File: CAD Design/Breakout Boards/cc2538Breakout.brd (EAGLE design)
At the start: 160 x 100 mm, 21 parts

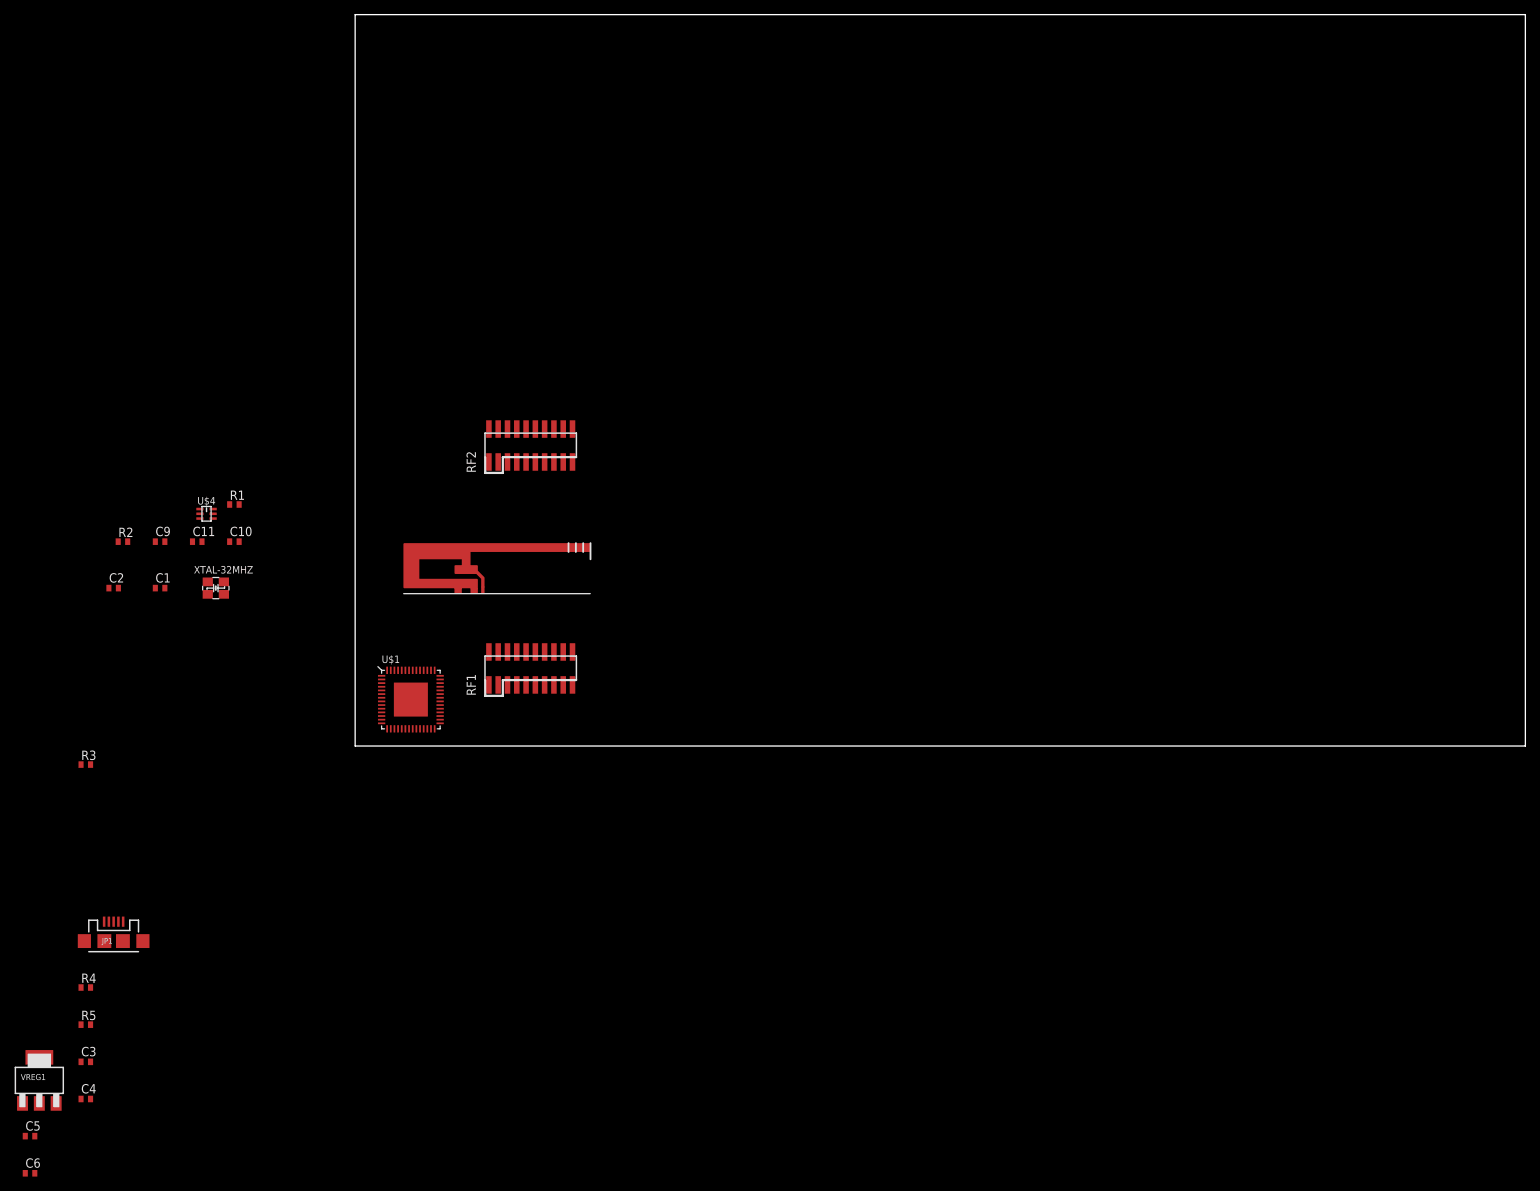
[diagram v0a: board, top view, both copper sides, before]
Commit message: cc2538EM schematic finished
Pin matched headers, added VCC decoupling bank.  Ready for board layout.
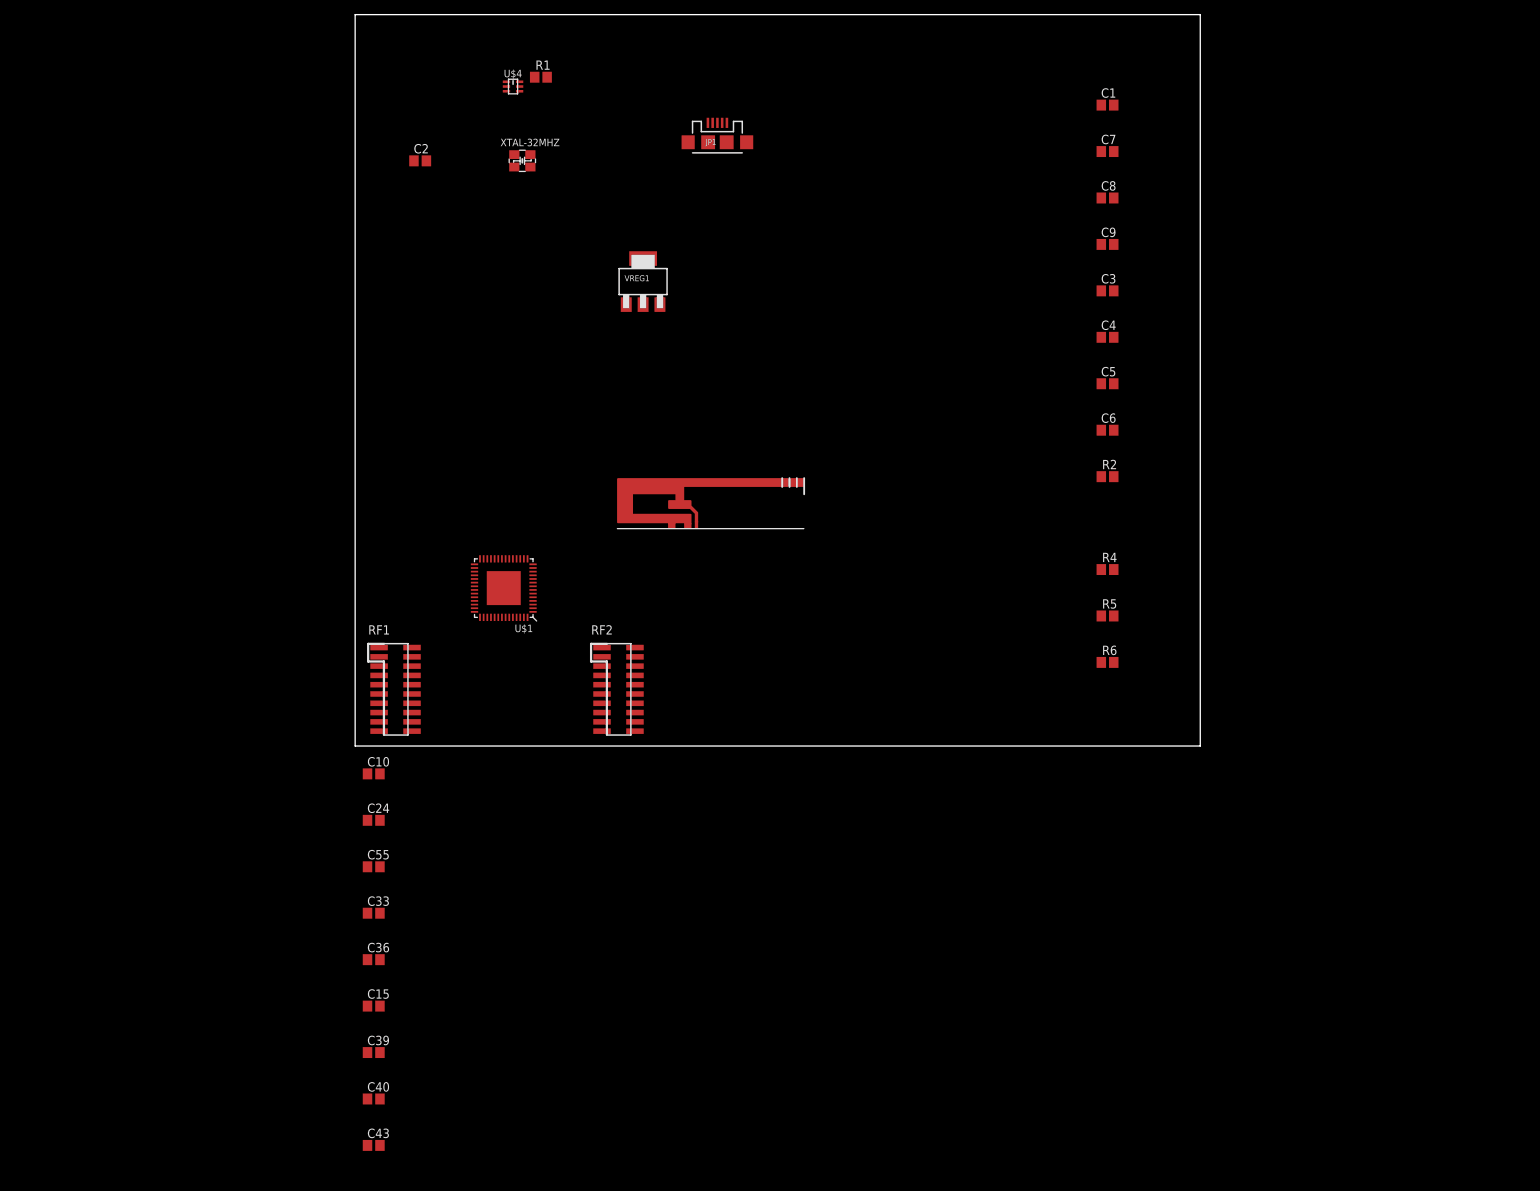
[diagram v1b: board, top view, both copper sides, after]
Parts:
- removed C11: 1nF, PCB 3.0.0:DISCRETE_C0402
- removed R3: 56k, PCB 3.0.0:RCL_R0402
- added C15, C24, C33, C36, C43: 100nF, resistor:C0805
- added C39, C55, C7, C8: 1uF, resistor:C0805
- added C40: 100pF, resistor:C0805
- added R6: 56k, resistor:R0805
- C1, C2, C3, C4: device PCB 3.0.0:DISCRETE_C0402 -> resistor:C0805
- C10: value 1uF -> 100nF; device PCB 3.0.0:DISCRETE_C0402 -> resistor:C0805
- C5, C6: value .1uF -> 1uF; device PCB 3.0.0:DISCRETE_C0402 -> resistor:C0805
- C9: value 1uF -> 1nF; device PCB 3.0.0:DISCRETE_C0402 -> resistor:C0805
- R1, R2, R4, R5: device PCB 3.0.0:RCL_R0402 -> resistor:R0805
- moved C5 179.7 mm to (102.9, 49.5)
- moved C6 179.0 mm to (102.9, 43.2)
- moved C3 175.0 mm to (102.9, 62.2)
- moved C4 174.2 mm to (102.9, 55.9)
- moved R4 150.9 mm to (102.9, 24.1)
- moved R5 150.5 mm to (102.9, 17.8)
- moved C1 145.4 mm to (102.9, 87.6)
- moved JP1 136.9 mm to (49.5, 82.5)
- moved VREG1 136.9 mm to (39.4, 63.5)
- moved C9 135.8 mm to (102.9, 68.6)
- moved R2 134.9 mm to (102.9, 36.8)
- moved C2 71.9 mm to (8.89, 80.0)
- moved U$4 71.9 mm to (21.6, 90.2)
- moved XTAL-32MHZ 71.9 mm to (22.9, 80.0)
- moved R1 71.9 mm to (25.4, 91.4)
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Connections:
- removed net N$12: U$1.23
- removed net N$15: U$1.22
- removed net N$16: U$1.21
- removed net N$17: U$1.20
- removed net N$18: U$1.19
- removed net N$19: U$1.18
- removed net N$21: U$1.16
- removed net N$22: U$1.5
- removed net N$23: U$1.6
- removed net N$24: U$1.7
- removed net N$25: U$1.8
- removed net N$26: U$1.9
- removed net N$27: U$1.11
- removed net N$28: U$1.12
- removed net N$29: U$1.13
- removed net N$3: U$1.31
- removed net N$31: U$1.54
- removed net N$32: U$1.53
- removed net N$33: U$1.52
- removed net N$34: U$1.51
- removed net N$35: U$1.50
- removed net N$36: U$1.49
- removed net N$37: U$1.48
- removed net N$39: U$1.47
- removed net N$4: U$1.30
- removed net N$40: U$1.46
- removed net N$44: R2.1
- removed net N$7: U$1.27
- removed net N$8: U$1.26
- removed net N$9: U$1.25
- new net I/O10: U$1.7, U$3.10
- new net I/O11: U$1.53, U$3.11
- new net I/O12: U$1.6, U$3.12
- new net I/O13: U$1.52, U$3.13
- new net I/O14: U$1.19, U$3.14
- new net I/O15: U$1.51, U$3.15
- new net I/O16: U$1.18, U$3.16
- new net I/O17: U$1.50, U$3.17
- new net I/O18: U$1.20, U$3.18
- new net I/O2: U$1.12, U$3.2
- new net I/O20: U$1.21, U$3.20
- new net I/O21: U$1.47, U$3.21
- new net I/O23: U$3.23
- new net I/O24: U$1.46, U$3.24
- new net I/O25: U$1.22, U$3.25
- new net I/O26: U$1.23, U$3.26
- new net I/O27: U$3.27
- new net I/O28: U$1.30, U$3.28
- new net I/O29: U$3.29
- new net I/O3: U$1.5, U$3.3
- new net I/O30: U$1.31, U$3.30
- new net I/O31: U$1.13, U$3.31
- new net I/O32: U$1.25, U$3.32
- new net I/O33: U$3.33
- new net I/O34: U$1.26, U$3.34
- new net I/O35: R2.1, U$3.35
- new net I/O36: U$1.27, U$3.36
- new net I/O37: U$1.49, U$3.37
- new net I/O38: U$1.29, U$3.38
- new net I/O39: U$1.48, U$3.39
- new net I/O4: U$1.11, U$3.4
- new net I/O5: U$1.54, U$3.5
- new net I/O6: U$1.9, U$3.6
- new net I/O7: U$1.16, U$3.7
- new net I/O8: U$1.8, U$3.8
- new net I/O9: U$1.17, U$3.9
- net GND: now also C15.2, C24.2, C3.1, C33.2, C36.2, C39.2, C4.2, C40.2, C43.2, C5.1, C55.2, C6.2, C7.2, C8.1, C9.1, U$1.PAD, U$3.1, U$3.19, U$3.22, U$3.40; no longer C11.2, C3.2, C4.1, C5.2, C6.1, C9.2
- net N$10: now also C8.2; no longer C9.1
- net N$11: now also C7.1; no longer C10.1
- net N$14: now also C9.2; no longer C11.1
- net N$30: now also R6.1; no longer R3.1
- net N$41: now also C3.2; no longer C3.1
- net N$42: now also C4.1, R6.2; no longer C4.2, R3.2
- net N$45: now also C6.1; no longer C6.2
- net VCC: now also C10.1, C15.1, C24.1, C33.1, C36.1, C39.1, C40.1, C43.1, C5.2, C55.1; no longer C5.1
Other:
- board size 160 x 100 mm -> 115.5 x 100 mm

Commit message: cc2538 Breakout, Board Layout upload1
Partial routing on microprocessor breakout, fixed wiring in antennae.
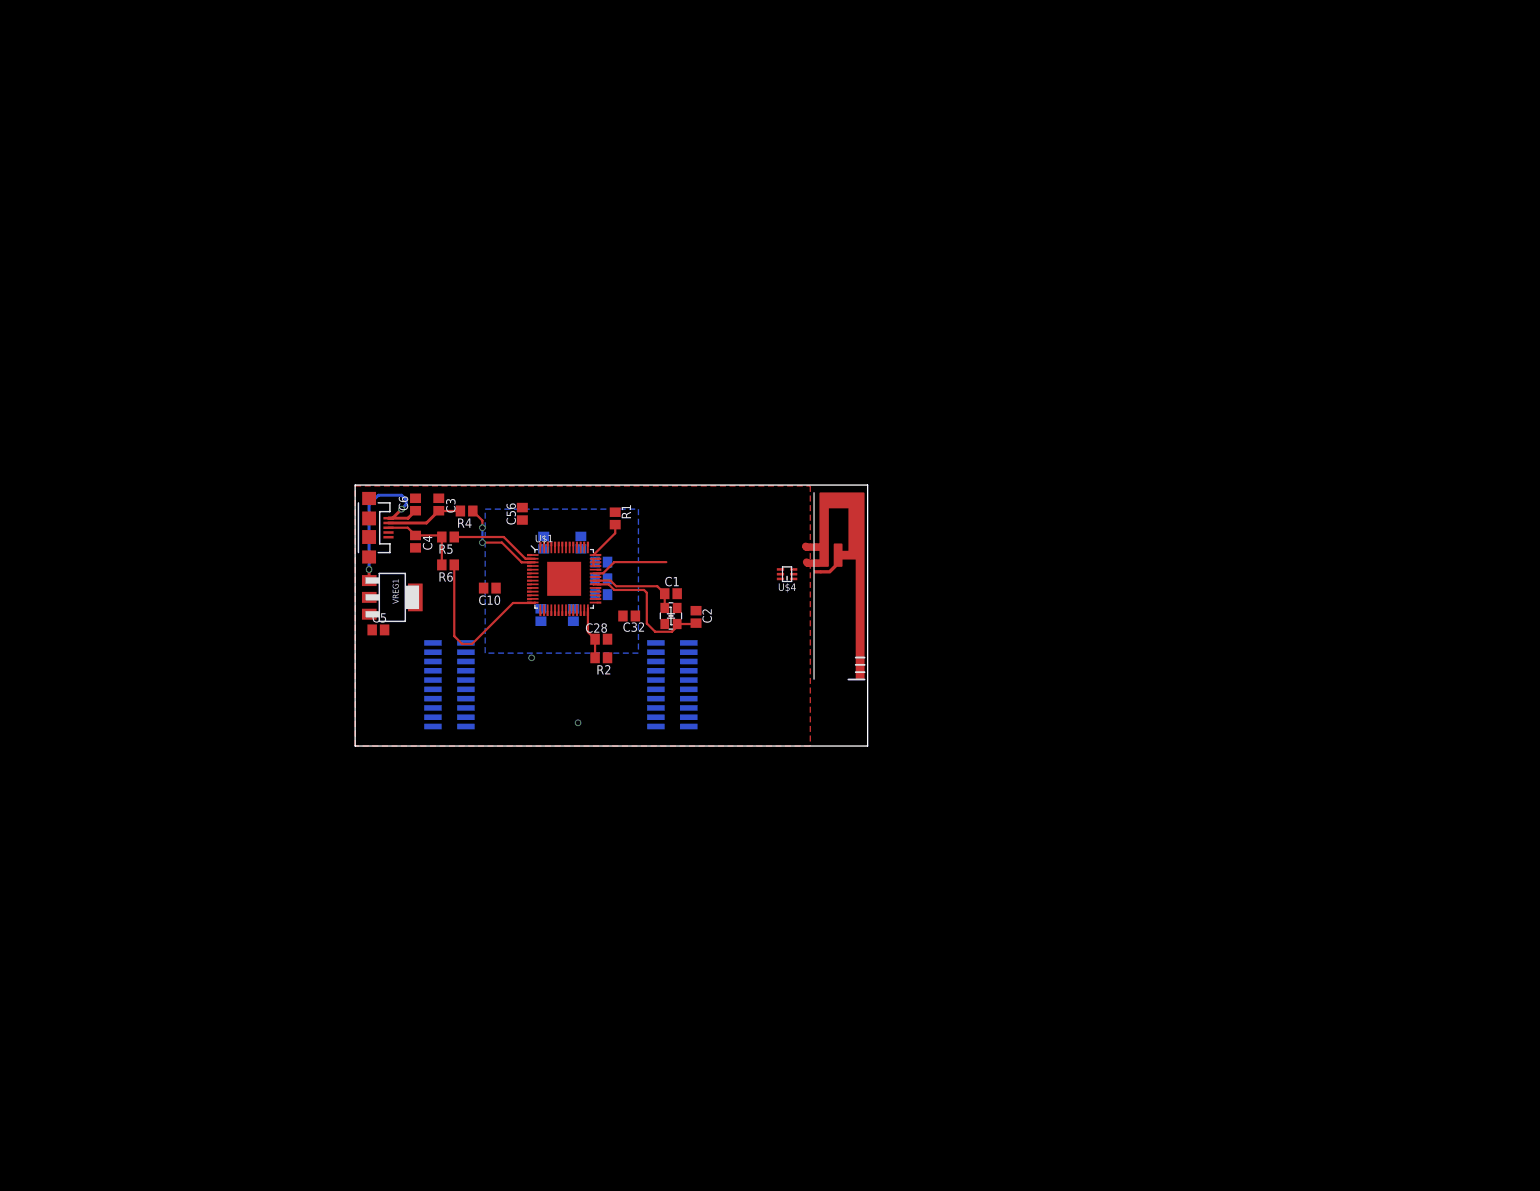
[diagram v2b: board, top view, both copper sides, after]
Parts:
- removed C40: 100pF, resistor:C0805
- removed C7, C8: 1uF, resistor:C0805
- removed C9: 1nF, resistor:C0805
- added C28: 1nF, resistor:C0805
- added C32, C56: 1uF, resistor:C0805
- U$1: value IC_CC2538 -> CC2538; device PCB 3.0.0:IC_QFN56 -> cc2538ext:QFN56-EXT
- moved C5 105.2 mm to (3.17, 15.9)
- moved C4 98.7 mm to (8.26, 27.9), turned to 270 degrees
- moved C3 96.0 mm to (11.4, 33.0), turned to 270 degrees
- moved C6 95.2 mm to (8.26, 33.0), turned to 90 degrees
- moved R6 91.2 mm to (12.7, 24.8), turned to 180 degrees
- moved R5 90.8 mm to (12.7, 28.6), turned to 180 degrees
- moved C1 89.6 mm to (43.2, 20.8)
- moved R4 88.0 mm to (15.2, 32.1), turned to 180 degrees
- moved C43 87.2 mm to (30.9, 27.8), flipped to the bottom, turned to 90 degrees
- moved U$4 76.5 mm to (59.1, 23.5), turned to 180 degrees
- moved C39 73.9 mm to (33.7, 25.1), flipped to the bottom
- moved R2 73.5 mm to (33.7, 12.1), turned to 180 degrees
- moved C2 72.9 mm to (46.6, 17.7), turned to 90 degrees
- moved JP1 71.0 mm to (1.91, 29.8), turned to 270 degrees
- moved XTAL-32MHZ 65.5 mm to (43.2, 17.8), turned to 90 degrees
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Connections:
- net GND: now also C28.1, C32.2, C56.1, U$2.GND, U$2.GND@1; no longer C40.2, C7.2, C8.1, C9.1, U$2.FEED
- net N$10: now also C56.2; no longer C8.2
- net N$11: now also C32.1; no longer C7.1
- net N$14: now also C28.2; no longer C9.2
- net N$2: now also U$2.FEED; no longer U$2.GND, U$2.GND@1
- net VCC: no longer C40.1
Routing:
- net N$45: track 0.00 -> 24.2 mm, vias 0 -> 2
- net N$30: track 0.00 -> 23.5 mm
- net N$1: track 0.00 -> 19.9 mm
- net N$43: track 0.00 -> 13.2 mm, vias 0 -> 2
- net XOSC32N_Q2: track 0.00 -> 12.4 mm
- net N$38: track 0.00 -> 12.3 mm
- net N$42: track 0.00 -> 11.6 mm
- net N$5: track 0.00 -> 10.6 mm
- net N$41: track 0.00 -> 10.5 mm
- net N$14: track 0.00 -> 7.20 mm
- net N$13: track 0.00 -> 5.39 mm
- net GND: track 0.00 -> 3.01 mm, vias 0 -> 2
- net VCC: track 0.00 -> 1.00 mm
- added copper zone on layer 1, net GND
- added copper zone on layer 16, net GND
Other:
- board size 115.5 x 100 mm -> 70.1 x 35.7 mm

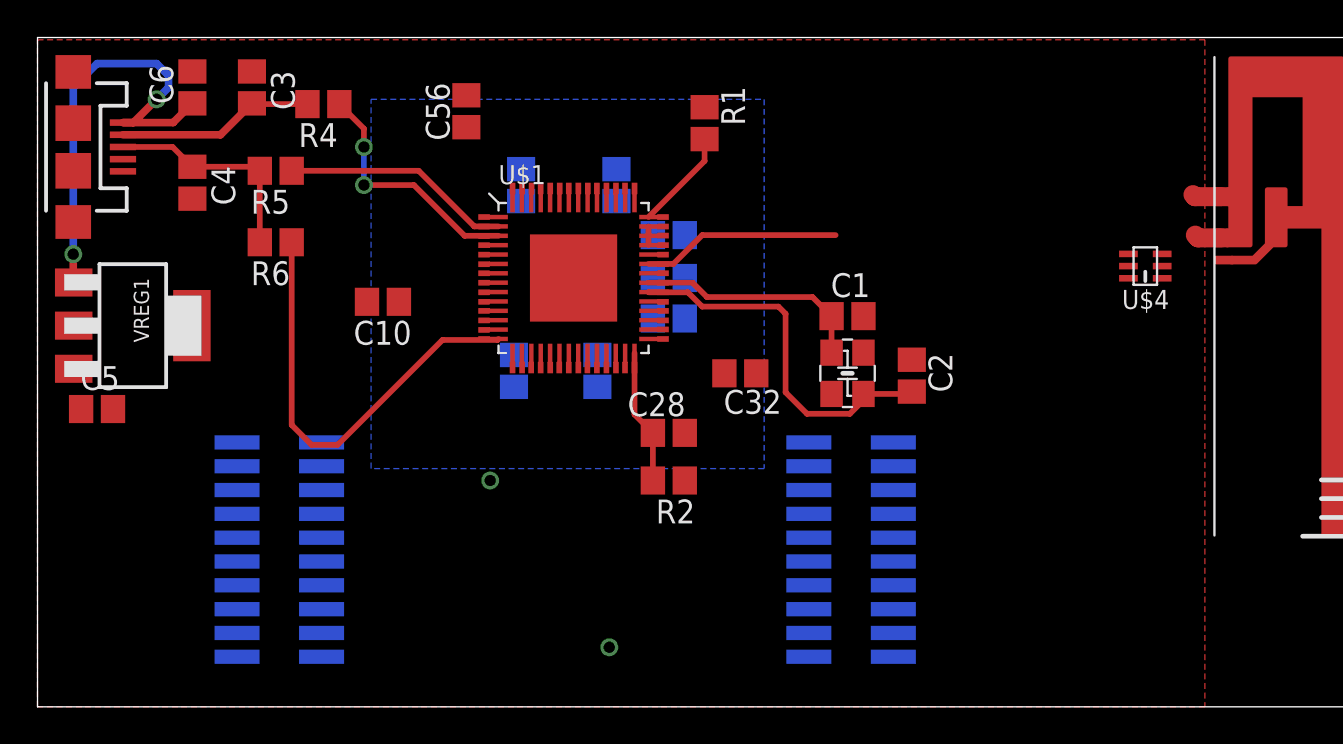
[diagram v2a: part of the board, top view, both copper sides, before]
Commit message: cc2538 breakout. update#2
Routed antennae, better xtal routing. Most of power routed. I/O still
to come.
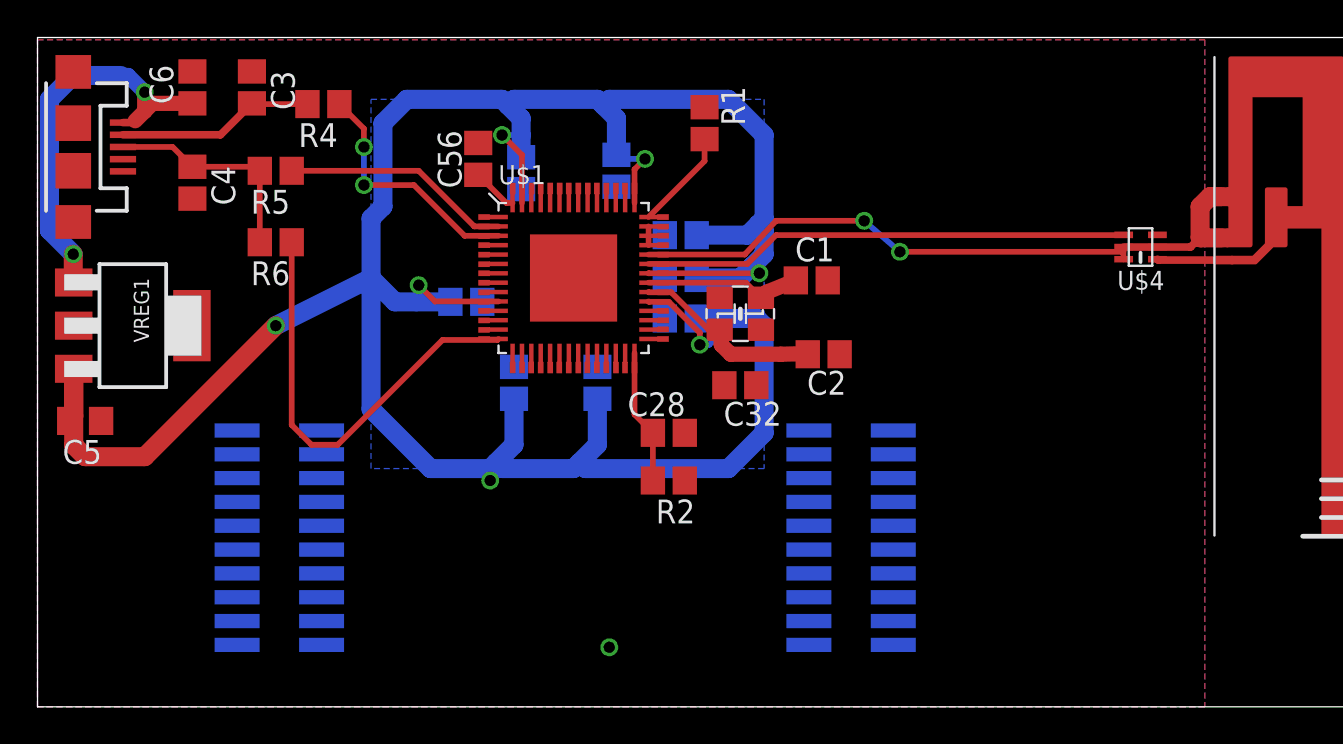
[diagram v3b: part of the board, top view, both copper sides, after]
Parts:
- moved XTAL-32MHZ 6.54 mm to (37.5, 21.0), turned to 0 degrees
- moved C2 4.84 mm to (41.9, 18.8), turned to 0 degrees
- moved C10 4.45 mm to (22.9, 21.6), flipped to the bottom
- moved C1 2.69 mm to (41.3, 22.7)
- moved C56 2.62 mm to (23.5, 29.2)
- moved U$4 1.05 mm to (58.8, 24.5)
- moved C5 0.90 mm to (2.54, 15.2), turned to 180 degrees
- moved C43 0.76 mm to (30.9, 28.6), turned to 270 degrees
- moved C15 0.64 mm to (25.4, 17.3)
- moved C24 0.64 mm to (29.8, 17.3)
- moved C32 0.64 mm to (37.5, 17.1)
- moved C55 0.64 mm to (25.8, 28.4), turned to 270 degrees
- moved U$3 0.64 mm to (45.1, 2.54)
- moved C33 0.63 mm to (34.3, 20.7)
- moved C36 0.63 mm to (34.3, 22.9)
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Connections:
- new net ANT_GND: U$1.38, U$2.GND, U$2.GND@1, U$4.5, U$4.6
- net GND: no longer U$1.38, U$2.GND, U$2.GND@1, U$4.5, U$4.6
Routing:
- net VCC: track 1.00 -> 158.3 mm, vias 0 -> 6
- net ANT_GND: track 0.00 -> 35.8 mm, vias 0 -> 2
- net N$5: track 10.6 -> 26.0 mm
- net N$1: track 19.9 -> 10.5 mm
- net XOSC32N_Q2: track 12.4 -> 8.43 mm
- net N$2: track 0.00 -> 3.56 mm
- net GND: track 3.01 -> 0.00 mm
- net N$45: track 24.2 -> 21.4 mm
- net N$10: track 0.00 -> 2.45 mm
